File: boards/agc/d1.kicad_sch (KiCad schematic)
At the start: 3 parts

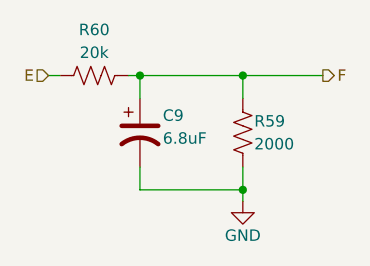
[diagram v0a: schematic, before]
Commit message: Add PSA switching modules and rework fine ref
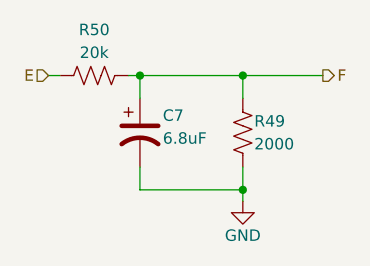
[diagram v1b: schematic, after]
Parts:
- renumbered C9 to C7, R59 to R49, R60 to R50
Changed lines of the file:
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@@
 (kicad_sch
-	(version 20231120)
+	(version 20250114)
 	(generator "eeschema")
-	(generator_version "8.0")
+	(generator_version "9.0")
 	(paper "A4")
 	(junction
@@
 		(shape output)
 		(at 118.11 66.04 0)
-		(fields_autoplaced yes)
 		(effects
 			(font
@@
 		(shape input)
 		(at 87.63 66.04 180)
-		(fields_autoplaced yes)
 		(effects
 			(font
@@
 		(on_board yes)
 		(dnp no)
-		(property "Reference" "R59"
+		(property "Reference" "R49"
 			(at 110.49 71.12 0)
 			(effects
@@
 		(on_board yes)
 		(dnp no)
-		(property "Reference" "R60"
+		(property "Reference" "R50"
 			(at 92.71 60.96 90)
 			(effects
@@
 		(on_board yes)
 		(dnp no)
-		(property "Reference" "C9"
+		(property "Reference" "C7"
 			(at 100.33 70.485 0)
 			(effects
@@
 		(on_board yes)
 		(dnp no)
-		(property "Reference" "#PWR050"
+		(property "Reference" "#PWR048"
 			(at 109.22 86.36 0)
 			(effects
